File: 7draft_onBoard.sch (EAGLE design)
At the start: 73 parts, among them IC3 74ABT125PW, IC4 MAX4466KS, J2 USB_MINI-B_DIGIKEY, Q1 NPN 40V 1A SOT-23

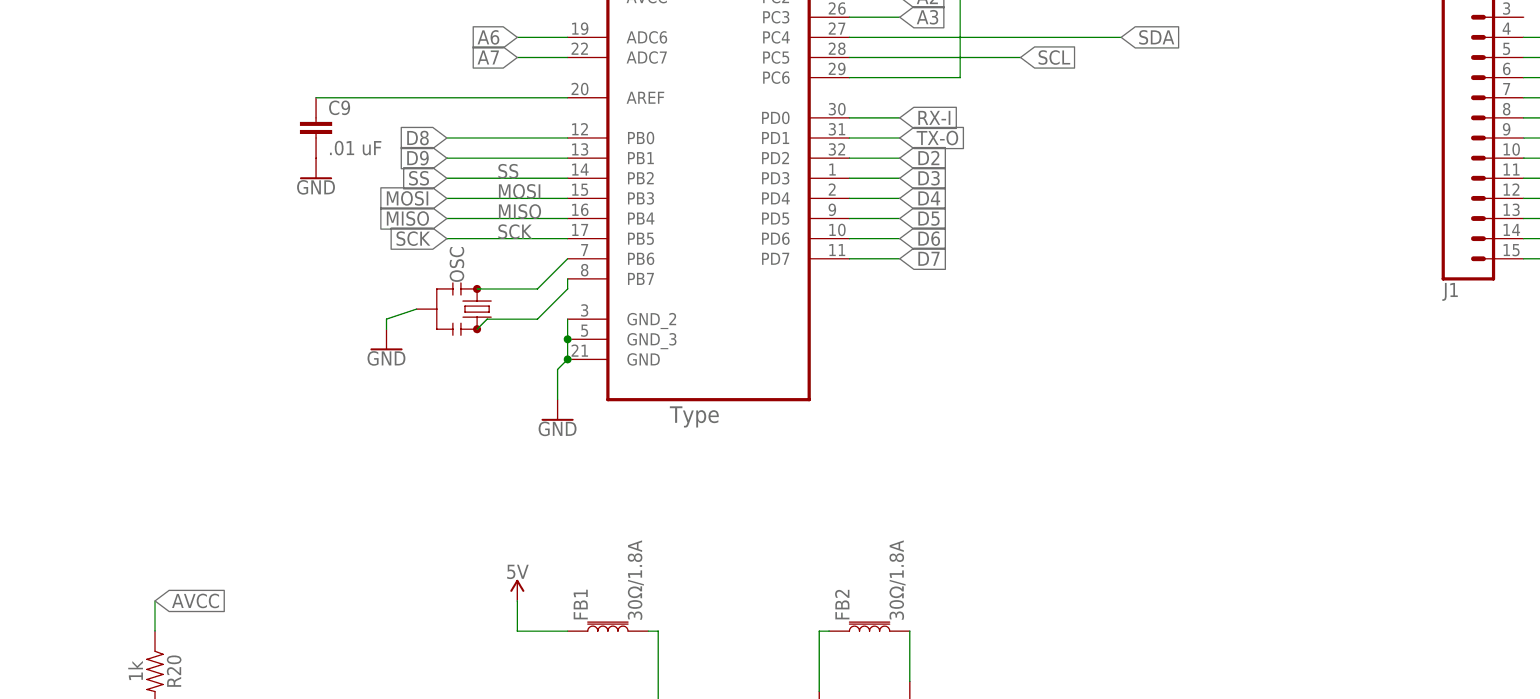
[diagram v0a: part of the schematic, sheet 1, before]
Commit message: added led's so we know when board has power and is able to blink
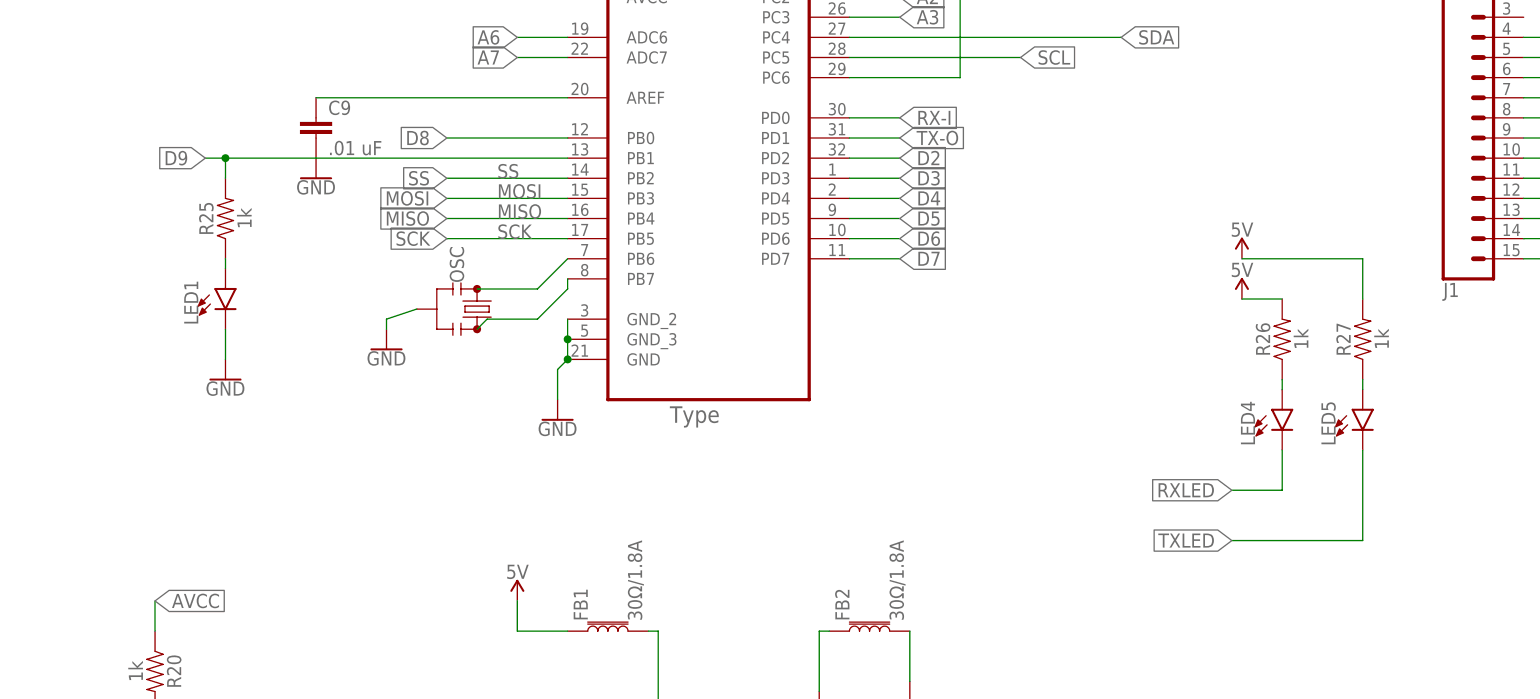
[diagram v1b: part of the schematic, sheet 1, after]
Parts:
- added LED1, LED4, LED5: (no value), SparkFun-LED:LED0603
- added R25, R26, R27: 1k, SparkFun-Retired:2.2MOHM-1/10W-5%(0603)
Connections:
- new net N$3: LED1.A, R25.1
- new net N$4: LED4.A, R26.1
- new net N$5: LED5.A, R27.1
- net 5V: now also R26.2, R27.2
- net D9: now also R25.2
- net GND: now also LED1.C
- net RXLED: now also LED4.C
- net TXLED: now also LED5.C
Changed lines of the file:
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@@
 <setting verticaltext="up"/>
 </settings>
-<grid distance="0.1" unitdist="inch" unit="inch" style="lines" multiple="1" display="no" altdistance="0.01" altunitdist="inch" altunit="inch"/>
+<grid distance="0.05" unitdist="inch" unit="inch" style="lines" multiple="1" display="yes" altdistance="0.005" altunitdist="inch" altunit="inch"/>
 <layers>
 <layer number="1" name="Top" color="4" fill="1" visible="no" active="no"/>
@@
 <part name="R23" library="SparkFun-Retired" deviceset="2.2MOHM-1/10W-5%(0603)" device="" value="470"/>
 <part name="R24" library="SparkFun-Retired" deviceset="2.2MOHM-1/10W-5%(0603)" device="" value="470"/>
+<part name="GND3" library="SparkFun-PowerSymbols" deviceset="GND" device=""/>
+<part name="LED1" library="SparkFun-LED" deviceset="LED" device="0603"/>
+<part name="R25" library="SparkFun-Retired" deviceset="2.2MOHM-1/10W-5%(0603)" device="" value="1k"/>
+<part name="LED4" library="SparkFun-LED" deviceset="LED" device="0603"/>
+<part name="R26" library="SparkFun-Retired" deviceset="2.2MOHM-1/10W-5%(0603)" device="" value="1k"/>
+<part name="LED5" library="SparkFun-LED" deviceset="LED" device="0603"/>
+<part name="R27" library="SparkFun-Retired" deviceset="2.2MOHM-1/10W-5%(0603)" device="" value="1k"/>
+<part name="SUPPLY5" library="SparkFun-PowerSymbols" deviceset="5V" device=""/>
+<part name="SUPPLY19" library="SparkFun-PowerSymbols" deviceset="5V" device=""/>
 </parts>
 <sheets>
@@
 <instance part="R23" gate="G$1" x="-500.38" y="-111.76"/>
 <instance part="R24" gate="G$1" x="-500.38" y="-124.46"/>
+<instance part="GND3" gate="1" x="-364.49" y="66.04"/>
+<instance part="LED1" gate="G$1" x="-364.49" y="77.47"/>
+<instance part="R25" gate="G$1" x="-364.49" y="86.36" rot="R90"/>
+<instance part="LED4" gate="G$1" x="-231.14" y="62.23"/>
+<instance part="R26" gate="G$1" x="-231.14" y="71.12" rot="R90"/>
+<instance part="LED5" gate="G$1" x="-220.98" y="62.23"/>
+<instance part="R27" gate="G$1" x="-220.98" y="71.12" rot="R90"/>
+<instance part="SUPPLY5" gate="G$1" x="-236.22" y="81.28"/>
+<instance part="SUPPLY19" gate="G$1" x="-236.22" y="76.2"/>
 </instances>
 <busses>
@@
 <label x="-436.88" y="200.66" size="1.778" layer="95" xref="yes"/>
 </segment>
+<segment>
+<pinref part="R27" gate="G$1" pin="2"/>
+<wire x1="-220.98" y1="76.2" x2="-220.98" y2="81.28" width="0.1524" layer="91"/>
+<wire x1="-220.98" y1="81.28" x2="-236.22" y2="81.28" width="0.1524" layer="91"/>
+<pinref part="SUPPLY5" gate="G$1" pin="5V"/>
+</segment>
+<segment>
+<pinref part="R26" gate="G$1" pin="2"/>
+<wire x1="-231.14" y1="76.2" x2="-236.22" y2="76.2" width="0.1524" layer="91"/>
+<pinref part="SUPPLY19" gate="G$1" pin="5V"/>
+</segment>
 </net>
 <net name="RESET" class="0">
@@
 <segment>
 <pinref part="ATMEGA328P-AU" gate="A" pin="PB1"/>
-<wire x1="-321.31" y1="93.98" x2="-336.55" y2="93.98" width="0.1524" layer="91"/>
-<label x="-336.55" y="93.98" size="1.778" layer="95" rot="R180" xref="yes"/>
+<label x="-367.03" y="93.98" size="1.778" layer="95" rot="R180" xref="yes"/>
+<wire x1="-321.31" y1="93.98" x2="-364.49" y2="93.98" width="0.1524" layer="91"/>
+<pinref part="R25" gate="G$1" pin="2"/>
+<wire x1="-364.49" y1="93.98" x2="-367.03" y2="93.98" width="0.1524" layer="91"/>
+<wire x1="-364.49" y1="93.98" x2="-364.49" y2="91.44" width="0.1524" layer="91"/>
+<junction x="-364.49" y="93.98"/>
 </segment>
 <segment>
@@
 <pinref part="GND44" gate="1" pin="GND"/>
 </segment>
+<segment>
+<pinref part="LED1" gate="G$1" pin="C"/>
+<pinref part="GND3" gate="1" pin="GND"/>
+<wire x1="-364.49" y1="72.39" x2="-364.49" y2="68.58" width="0.1524" layer="91"/>
+</segment>
 </net>
 <net name="IR_LED" class="0">
@@
 </segment>
 </net>
+<net name="N$3" class="0">
+<segment>
+<pinref part="LED1" gate="G$1" pin="A"/>
+<pinref part="R25" gate="G$1" pin="1"/>
+<wire x1="-364.49" y1="81.28" x2="-364.49" y2="80.01" width="0.1524" layer="91"/>
+</segment>
+</net>
+<net name="N$4" class="0">
+<segment>
+<pinref part="R26" gate="G$1" pin="1"/>
+<pinref part="LED4" gate="G$1" pin="A"/>
+<wire x1="-231.14" y1="66.04" x2="-231.14" y2="64.77" width="0.1524" layer="91"/>
+</segment>
+</net>
+<net name="N$5" class="0">
+<segment>
+<pinref part="R27" gate="G$1" pin="1"/>
+<pinref part="LED5" gate="G$1" pin="A"/>
+<wire x1="-220.98" y1="66.04" x2="-220.98" y2="64.77" width="0.1524" layer="91"/>
+</segment>
+</net>
+<net name="RXLED" class="0">
+<segment>
+<pinref part="LED4" gate="G$1" pin="C"/>
+<wire x1="-231.14" y1="57.15" x2="-231.14" y2="52.07" width="0.1524" layer="91"/>
+<wire x1="-231.14" y1="52.07" x2="-237.49" y2="52.07" width="0.1524" layer="91"/>
+<label x="-237.49" y="52.07" size="1.778" layer="95" rot="R180" xref="yes"/>
+</segment>
+</net>
+<net name="TXLED" class="0">
+<segment>
+<pinref part="LED5" gate="G$1" pin="C"/>
+<wire x1="-220.98" y1="57.15" x2="-220.98" y2="45.72" width="0.1524" layer="91"/>
+<wire x1="-220.98" y1="45.72" x2="-237.49" y2="45.72" width="0.1524" layer="91"/>
+<label x="-237.49" y="45.72" size="1.778" layer="95" rot="R180" xref="yes"/>
+</segment>
+</net>

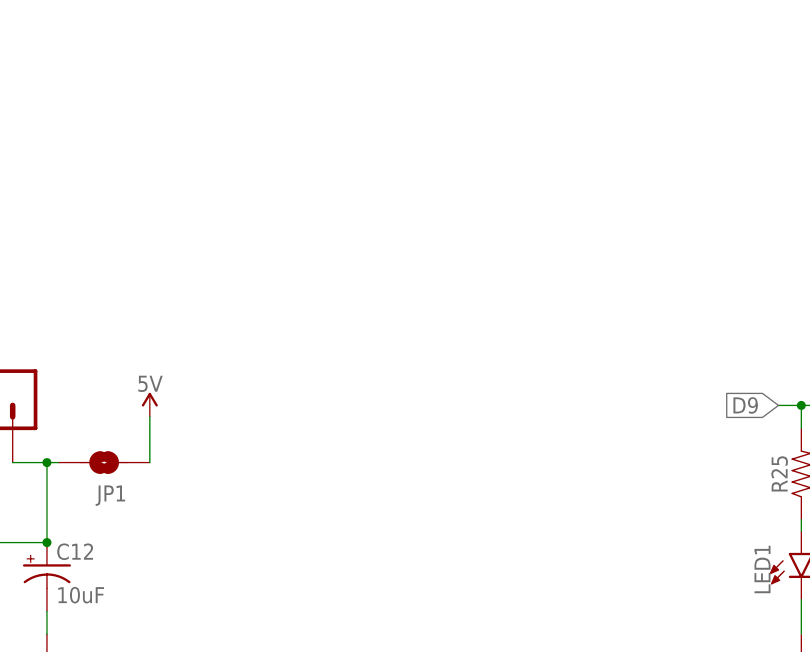
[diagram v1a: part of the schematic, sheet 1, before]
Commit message: added leds for RX, TX, power
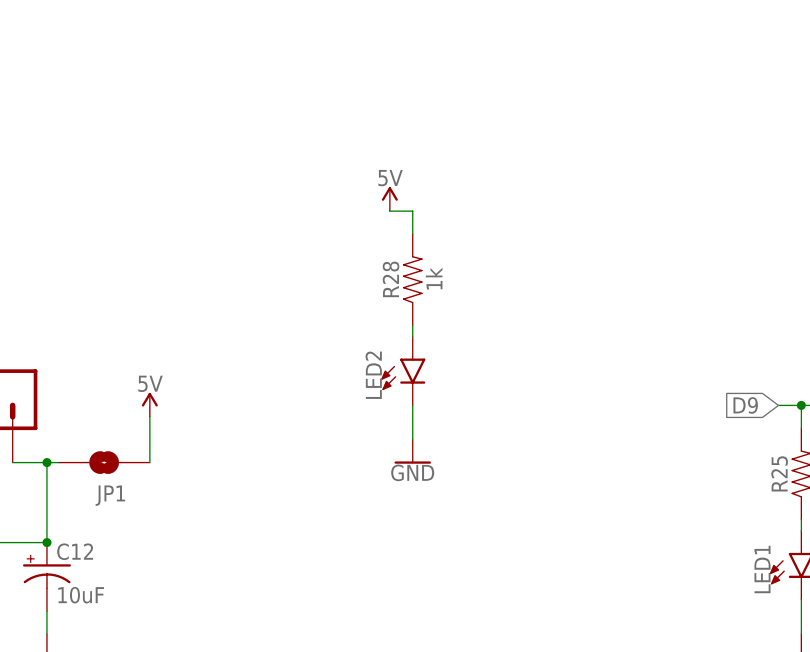
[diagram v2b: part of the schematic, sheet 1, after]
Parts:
- added LED2: (no value), SparkFun-LED:LED0603
- added R28: 1k, SparkFun-Retired:2.2MOHM-1/10W-5%(0603)
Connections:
- new net N$7: LED2.A, R28.1
- net 5V: now also R28.2
- net GND: now also LED2.C
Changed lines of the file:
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@@
 <part name="SUPPLY5" library="SparkFun-PowerSymbols" deviceset="5V" device=""/>
 <part name="SUPPLY19" library="SparkFun-PowerSymbols" deviceset="5V" device=""/>
+<part name="GND4" library="SparkFun-PowerSymbols" deviceset="GND" device=""/>
+<part name="LED2" library="SparkFun-LED" deviceset="LED" device="0603"/>
+<part name="R28" library="SparkFun-Retired" deviceset="2.2MOHM-1/10W-5%(0603)" device="" value="1k"/>
+<part name="SUPPLY20" library="SparkFun-PowerSymbols" deviceset="5V" device=""/>
 </parts>
 <sheets>
@@
 <instance part="SUPPLY5" gate="G$1" x="-236.22" y="81.28"/>
 <instance part="SUPPLY19" gate="G$1" x="-236.22" y="76.2"/>
+<instance part="GND4" gate="1" x="-407.67" y="87.63"/>
+<instance part="LED2" gate="G$1" x="-407.67" y="99.06"/>
+<instance part="R28" gate="G$1" x="-407.67" y="107.95" rot="R90"/>
+<instance part="SUPPLY20" gate="G$1" x="-410.21" y="115.57"/>
 </instances>
 <busses>
@@
 <pinref part="SUPPLY19" gate="G$1" pin="5V"/>
 </segment>
+<segment>
+<pinref part="R28" gate="G$1" pin="2"/>
+<wire x1="-407.67" y1="115.57" x2="-410.21" y2="115.57" width="0.1524" layer="91"/>
+<wire x1="-407.67" y1="115.57" x2="-407.67" y2="113.03" width="0.1524" layer="91"/>
+<pinref part="SUPPLY20" gate="G$1" pin="5V"/>
+</segment>
 </net>
 <net name="RESET" class="0">
@@
 <wire x1="-364.49" y1="72.39" x2="-364.49" y2="68.58" width="0.1524" layer="91"/>
 </segment>
+<segment>
+<pinref part="LED2" gate="G$1" pin="C"/>
+<pinref part="GND4" gate="1" pin="GND"/>
+<wire x1="-407.67" y1="93.98" x2="-407.67" y2="90.17" width="0.1524" layer="91"/>
+</segment>
 </net>
 <net name="IR_LED" class="0">
@@
 </segment>
 </net>
+<net name="N$7" class="0">
+<segment>
+<pinref part="LED2" gate="G$1" pin="A"/>
+<pinref part="R28" gate="G$1" pin="1"/>
+<wire x1="-407.67" y1="102.87" x2="-407.67" y2="101.6" width="0.1524" layer="91"/>
+</segment>
+</net>
